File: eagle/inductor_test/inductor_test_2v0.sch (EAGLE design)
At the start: 22 parts, among them J1 MA02-1_ROUND

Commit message: added new amplifiers for inductor inspector
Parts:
- removed L10, L6, L7, L8, L9: (no value), rcl:L-USL0805
- added C1, C2, C3: (no value), rcl:C-EUC0603
- added R2, R3, R4, R5, R6, R7: (no value), rcl:R-US_R0603
- added U1: MCP6V3, powerfilm:MCP6V3
- added U2, U3: OPA333, powerfilm:MCP6V3
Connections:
- new net +3V3: C1.1, C2.1, C3.1, U1.VCC, U2.VCC, U3.VCC
- new net GND: C1.2, C2.2, C3.2, R4.1, R5.1, R7.1, U1.VSS, U2.VSS, U3.VSS
- new net L_SIG: U1.IN+, U2.IN+, U3.IN+
- new net N$3: R6.1, R7.2, U3.IN-
- new net N$4: R2.1, R4.2, U1.IN-
- new net N$6: R3.1, R5.2, U2.IN-
- new net OUT_MCP6V3: R2.2, U1.OUT
- new net OUT_OPA333: R3.2, R6.2, U2.OUT, U3.OUT
- net C1P1: no longer L14.1
- net C2P1: no longer L15.1
- net L10P1: no longer L10.1
- net L10P2: no longer L10.2
- net L11P1: now also L1.1, L12.1, L13.1, L14.1, L15.1, L2.1, L3.1, L4.1, L5.1
- net L12P1: no longer L12.1
- net L13P1: no longer L13.1
- net L1P1: no longer L1.1
- net L2P1: no longer L2.1
- net L3P1: no longer L3.1
- net L4P1: no longer L4.1
- net L5P1: no longer L5.1
- net L6P1: no longer L6.1
- net L6P2: no longer L6.2
- net L7P1: no longer L7.1
- net L7P2: no longer L7.2
- net L8P1: no longer L8.1
- net L8P2: no longer L8.2
- net L9P1: no longer L9.1
- net L9P2: no longer L9.2

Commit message: more work in inductor board
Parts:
- added C4, C5, C6, C7, C8: (no value), rcl:C-EUC0603
- added R10, R11, R8, R9: (no value), rcl:R-US_R0603
- added U4, U6: MAX4238, powerfilm:MAX4238
- added U5: LMP2014, powerfilm:LMP2014
- added U7: OPA376, powerfilm:MCP6V3
- U2: DIGIKEY (none) -> 296-19547-1-ND
- U3: value OPA333 -> OPA376; DIGIKEY (none) -> 296-22191-1-ND
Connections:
- new net N$5: R8.2, R9.1, U4.IN-
- new net N$7: C8.2, U7.IN+
- new net N$8: R10.1, R11.2, U5G1.IN-
- new net N$9: C6.2, U6.IN+
- new net OUT1_LMP2014: R10.2, U5G1.OUT
- new net OUT1_MAX4238: C6.1, R9.2, U4.OUT
- new net OUT1_OPA376: C8.1, R6.2, U3.OUT
- net +3V3: now also C4.1, C5.1, U4.VCC, U5G1.VCC
- net GND: now also C4.2, C5.2, R11.1, R8.1, U4.VSS, U5G1.VSS
- net L_SIG: now also U4.IN+
- net OUT_OPA333: no longer R6.2, U3.OUT

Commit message: added new amplifier configuration
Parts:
- removed J1, SV2, SV3: MA02-1_ROUND, con-lstb:MA02-1_ROUND
- removed L11, L12, L13, L14, L15: (no value), rcl:L-USL0805
- removed SV1: (no value), con-lstb:MA13-2BARE
- removed TP1, TP2: TP_STD, skyspecs:TP_STD
- removed U2: OPA333, powerfilm:MCP6V3
- removed U6: MAX4238, powerfilm:MAX4238
- removed U7: OPA376, powerfilm:MCP6V3
- added C10, C11, C12, C13, C9: (no value), rcl:C-EUC0402
- added C14: (no value), rcl:C-EUC0603
- added R12, R13, R14, R15, R16, R17, R18, R19: (no value), rcl:R-US_R0402
- C1, C2, C6, C7, C8: device rcl:C-EUC0603 -> rcl:C-EUC0402
- R1: device rcl:R-US_R0603 -> rcl:R-US_R0402; DIGIKEY P49.9HCT-ND -> (none); DIGIKEY_2 P220JCT-ND -> (none)
- R10, R11, R5, R6, R7, R8, R9: device rcl:R-US_R0603 -> rcl:R-US_R0402
- R2: value (none) -> 200; device rcl:R-US_R0603 -> rcl:R-US_R0402
- R3: value (none) -> 1M; device rcl:R-US_R0603 -> rcl:R-US_R0402
- R4: value (none) -> 75; device rcl:R-US_R0603 -> rcl:R-US_R0402
- U1: value MCP6V3 -> OPA2369; device powerfilm:MCP6V3 -> powerfilm:OPA2369
- U3: value OPA376 -> SC70
- U4: value MAX4238 -> SOT-23-6
- U5: value LMP2014 -> TSSOP-14
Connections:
- net OUT1_MAX4238 renamed OUT1_SOT23
- net OUT1_OPA376 renamed OUT1_SC70
- removed net C1P1: SV2.1
- removed net C1P2: L14.2, SV2.2
- removed net C2P1: SV3.2
- removed net C2P2: L15.2, SV3.1
- removed net L10P1: SV1.8
- removed net L10P2: SV1.7
- removed net L11P1: L1.1, L11.1, L12.1, L13.1, L14.1, L15.1, L2.1, L3.1, L4.1, L5.1, SV1.5
- removed net L11P2: L11.2, SV1.6
- removed net L12P1: SV1.4
- removed net L12P2: L12.2, SV1.3
- removed net L13P1: SV1.1
- removed net L13P2: L13.2, SV1.2
- removed net L1P1: SV1.25
- removed net L2P1: SV1.24
- removed net L2P2: L2.2, SV1.23
- removed net L3P1: SV1.21
- removed net L3P2: L3.2, SV1.22
- removed net L4P1: SV1.20
- removed net L4P2: L4.2, SV1.19
- removed net L5P1: SV1.17
- removed net L5P2: L5.2, SV1.18
- removed net L6P1: SV1.16
- removed net L6P2: SV1.15
- removed net L7P1: SV1.13
- removed net L7P2: SV1.14
- removed net L8P1: SV1.12
- removed net L8P2: SV1.11
- removed net L9P1: SV1.9
- removed net L9P2: SV1.10
- removed net OUT1_LMP2014: R10.2, U5G1.OUT
- removed net OUT_MCP6V3: R2.2, U1.OUT
- removed net OUT_OPA333: R3.2, U2.OUT
- new net N$10: C6.2, R12.1, U1G$2.IN+
- new net N$11: C11.1, R15.1
- new net N$12: C7.2, R13.1, U5G2.IN+
- new net N$14: R16.1, R17.2, U1G$2.IN-
- new net N$15: C12.1, R17.1
- new net N$17: R18.1, R19.2, U5G2.IN-
- new net N$18: C13.1, R19.1
- new net OUT1_TSSOP14: C7.1, R10.2, U5G1.OUT
- new net OUT2_SC70: R14.2, U1G$1.OUT
- new net OUT2_SOT23: R16.2, U1G$2.OUT
- new net OUT2_TSSOP14: R18.2, U5G2.OUT
- new net VREF_1V65: R5.2
- new net VREF_V054: R1.2, R12.2, R13.2
- net +3V3: now also C14.1, R3.1, U1G$1.VCC; no longer C1.1, C2.1, U1.VCC, U2.VCC
- net GND: now also C10.2, C11.2, C12.2, C13.2, C14.2, C9.2, U1G$1.VSS; no longer C1.2, R11.1, R5.1, R7.1, R8.1, U1.VSS, U2.VSS
- net L1P2: now also L2.2, L3.2, L4.2, L5.2, R2.1, R3.2, R4.2; no longer SV1.26
- net L_SIG: now also C1.2, R5.1, U5G1.IN+; no longer U1.IN+, U2.IN+
- net N$1: now also C10.1, R11.1; no longer J1.2, R1.1, TP1.P$1
- net N$2: now also C9.1, R8.1; no longer J1.1, R1.2, TP2.P$1
- net N$4: now also C1.1, L1.1, L2.1, L3.1, L4.1, L5.1, R2.2; no longer R2.1, R4.2, U1.IN-
- net N$6: now also C2.1, R7.1; no longer R3.1, R5.2, U2.IN-
- net N$7: now also R1.1, U1G$1.IN+; no longer U7.IN+
- net N$9: now also R14.1, R15.2, U1G$1.IN-; no longer C6.2, U6.IN+
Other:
- note added: "New Configuration:"
- note added: "Old Configuration:"

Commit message: added all components for inductor inspector
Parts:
- added C15: (no value), rcl:C-EUC0402
- added R20, R21, R22, R23: (no value), rcl:R-US_R0402
- added TP1, TP10, TP11, TP12, TP13, TP14, TP2, TP3, TP4, TP5, TP6, TP7, TP8, TP9: TP_MULT, skyspecs:TP_MULT
- added U2: OPA2369, powerfilm:OPA2369
- C3: device rcl:C-EUC0603 -> rcl:C-EUC0402
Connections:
- new net N$13: R22.1, R23.2, U2G$2.IN+
- new net N$16: R20.2, R21.1, U2G$1.IN+
- net +3V3: now also C15.1, R21.2, R22.2, U2G$1.VCC
- net GND: now also C15.2, R20.1, R23.1, TP10.P$1, TP11.P$1, TP12.P$1, TP13.P$1, TP14.P$1, TP9.P$1, U2G$1.VSS
- net OUT1_SC70: now also TP1.P$1
- net OUT1_SOT23: now also TP3.P$1
- net OUT1_TSSOP14: now also TP5.P$1
- net OUT2_SC70: now also TP2.P$1
- net OUT2_SOT23: now also TP4.P$1
- net OUT2_TSSOP14: now also TP6.P$1
- net VREF_1V65: now also TP7.P$1, U2G$1.IN-, U2G$1.OUT
- net VREF_V054: now also TP8.P$1, U2G$2.IN-, U2G$2.OUT

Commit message: all components added for inductor inspector
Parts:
- removed TP14: TP_MULT, skyspecs:TP_MULT
- added C16: 22pF, rcl:C-EUC0402_SM
- added C17: 4.7uF, rcl:C-EUC0402_SM
- added C18, C19: 0.1uF, rcl:C-EUC0402_SM
- added C20, C21: 22uF, rcl:C-EUC0603_SM
- added C22: 0.1uF, rcl:C-EUC0603
- added J1: MA02-1, con-lstb:MA02-1
- added L6: 10uH, rcl:L-USL0805
- added R24: 560k, rcl:R-US_R0402_SM
- added R25: 180k, rcl:R-US_R0402_SM
- added R26: 1 1%, rcl:R-US_R0603_SM
- added R27, R28: 10k, rcl:R-US_R0603
- added R29, R30: 10, rcl:R-US_R0603
- added TP16: TP_MULT, skyspecs:TP_MULT
- added U6: TPS62122, powerfilm:TPS62122
- added U7: MAX9910, powerfilm:MAX9910
- C14, C4, C5: device rcl:C-EUC0603 -> rcl:C-EUC0402
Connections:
- new net N$19: C16.2, R24.1, R25.2, U6.FB
- new net N$20: L6.2, U6.SW
- new net N$21: R28.1, R29.2, U7.IN+
- new net N$22: R27.1, R30.2, U7.IN-
- new net N$23: R27.2, TP16.P$1, U7.OUT
- new net VCC: C17.1, C18.1, J1.1, U6.EN, U6.VIN
- new net VS+: C16.1, C19.1, C20.1, L6.1, R24.2, R26.1, R29.1, U6.VOUT
- net +3V3: now also C21.1, C22.1, R26.2, R30.1, U7.VCC
- net GND: now also C17.2, C18.2, C19.2, C20.2, C21.2, C22.2, J1.2, R25.1, R28.2, U6.GND, U7.VSS; no longer TP14.P$1

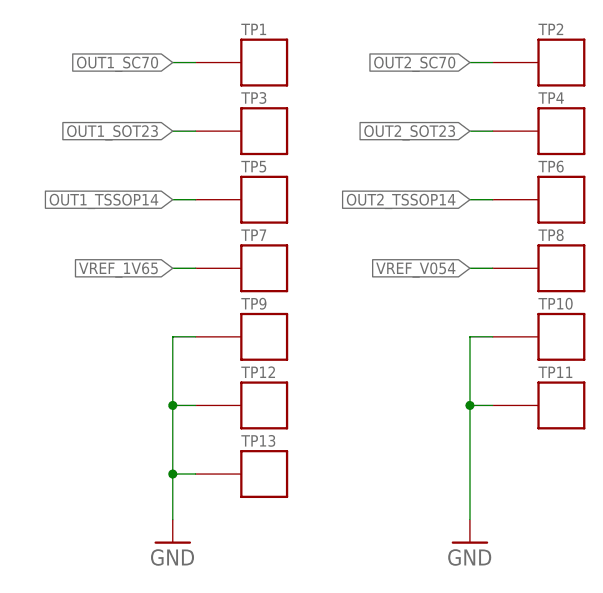
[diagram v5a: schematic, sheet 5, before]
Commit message: 23 airwires left
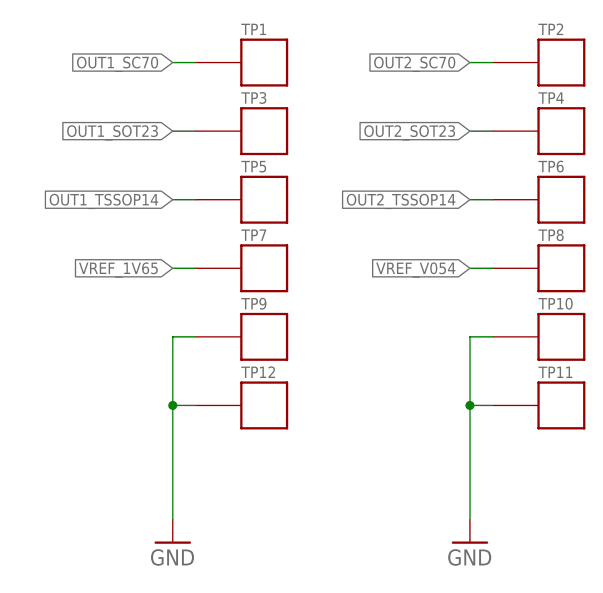
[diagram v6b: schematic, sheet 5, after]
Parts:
- removed TP13: TP_MULT, skyspecs:TP_MULT
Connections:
- net GND: no longer TP13.P$1
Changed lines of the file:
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@@
 <?xml version="1.0" encoding="utf-8"?>
 <!DOCTYPE eagle SYSTEM "eagle.dtd">
-<eagle version="6.3">
+<eagle version="6.5.0">
 <drawing>
 <settings>
@@
 <grid distance="0.1" unitdist="inch" unit="inch" style="lines" multiple="1" display="no" altdistance="0.01" altunitdist="inch" altunit="inch"/>
 <layers>
-<layer number="1" name="Top" color="4" fill="1" visible="yes" active="no"/>
-<layer number="2" name="Route2" color="1" fill="3" visible="yes" active="no"/>
-<layer number="3" name="Route3" color="4" fill="3" visible="yes" active="no"/>
-<layer number="4" name="Route4" color="1" fill="4" visible="yes" active="no"/>
-<layer number="5" name="Route5" color="4" fill="4" visible="yes" active="no"/>
-<layer number="6" name="Route6" color="1" fill="8" visible="yes" active="no"/>
-<layer number="7" name="Route7" color="4" fill="8" visible="yes" active="no"/>
-<layer number="8" name="Route8" color="1" fill="2" visible="yes" active="no"/>
-<layer number="9" name="Route9" color="4" fill="2" visible="yes" active="no"/>
-<layer number="10" name="Route10" color="1" fill="7" visible="yes" active="no"/>
-<layer number="11" name="Route11" color="4" fill="7" visible="yes" active="no"/>
-<layer number="12" name="Route12" color="1" fill="5" visible="yes" active="no"/>
-<layer number="13" name="Route13" color="4" fill="5" visible="yes" active="no"/>
-<layer number="14" name="Route14" color="1" fill="6" visible="yes" active="no"/>
-<layer number="15" name="Route15" color="4" fill="6" visible="yes" active="no"/>
-<layer number="16" name="Bottom" color="1" fill="1" visible="yes" active="no"/>
-<layer number="17" name="Pads" color="2" fill="1" visible="yes" active="no"/>
-<layer number="18" name="Vias" color="2" fill="1" visible="yes" active="no"/>
-<layer number="19" name="Unrouted" color="6" fill="1" visible="yes" active="no"/>
-<layer number="20" name="Dimension" color="15" fill="1" visible="yes" active="no"/>
-<layer number="21" name="tPlace" color="7" fill="1" visible="yes" active="no"/>
-<layer number="22" name="bPlace" color="7" fill="1" visible="yes" active="no"/>
-<layer number="23" name="tOrigins" color="15" fill="1" visible="yes" active="no"/>
-<layer number="24" name="bOrigins" color="15" fill="1" visible="yes" active="no"/>
-<layer number="25" name="tNames" color="7" fill="1" visible="yes" active="no"/>
-<layer number="26" name="bNames" color="7" fill="1" visible="yes" active="no"/>
-<layer number="27" name="tValues" color="7" fill="1" visible="yes" active="no"/>
-<layer number="28" name="bValues" color="7" fill="1" visible="yes" active="no"/>
+<layer number="1" name="Top" color="4" fill="1" visible="no" active="no"/>
+<layer number="2" name="Route2" color="1" fill="3" visible="no" active="no"/>
+<layer number="3" name="Route3" color="4" fill="3" visible="no" active="no"/>
+<layer number="4" name="Route4" color="1" fill="4" visible="no" active="no"/>
+<layer number="5" name="Route5" color="4" fill="4" visible="no" active="no"/>
+<layer number="6" name="Route6" color="1" fill="8" visible="no" active="no"/>
+<layer number="7" name="Route7" color="4" fill="8" visible="no" active="no"/>
+<layer number="8" name="Route8" color="1" fill="2" visible="no" active="no"/>
+<layer number="9" name="Route9" color="4" fill="2" visible="no" active="no"/>
+<layer number="10" name="Route10" color="1" fill="7" visible="no" active="no"/>
+<layer number="11" name="Route11" color="4" fill="7" visible="no" active="no"/>
+<layer number="12" name="Route12" color="1" fill="5" visible="no" active="no"/>
+<layer number="13" name="Route13" color="4" fill="5" visible="no" active="no"/>
+<layer number="14" name="Route14" color="1" fill="6" visible="no" active="no"/>
+<layer number="15" name="Route15" color="4" fill="6" visible="no" active="no"/>
+<layer number="16" name="Bottom" color="1" fill="1" visible="no" active="no"/>
+<layer number="17" name="Pads" color="2" fill="1" visible="no" active="no"/>
+<layer number="18" name="Vias" color="2" fill="1" visible="no" active="no"/>
+<layer number="19" name="Unrouted" color="6" fill="1" visible="no" active="no"/>
+<layer number="20" name="Dimension" color="15" fill="1" visible="no" active="no"/>
+<layer number="21" name="tPlace" color="7" fill="1" visible="no" active="no"/>
+<layer number="22" name="bPlace" color="7" fill="1" visible="no" active="no"/>
+<layer number="23" name="tOrigins" color="15" fill="1" visible="no" active="no"/>
+<layer number="24" name="bOrigins" color="15" fill="1" visible="no" active="no"/>
+<layer number="25" name="tNames" color="7" fill="1" visible="no" active="no"/>
+<layer number="26" name="bNames" color="7" fill="1" visible="no" active="no"/>
+<layer number="27" name="tValues" color="7" fill="1" visible="no" active="no"/>
+<layer number="28" name="bValues" color="7" fill="1" visible="no" active="no"/>
 <layer number="29" name="tStop" color="7" fill="3" visible="no" active="no"/>
 <layer number="30" name="bStop" color="7" fill="6" visible="no" active="no"/>
@@
 <layer number="35" name="tGlue" color="7" fill="4" visible="no" active="no"/>
 <layer number="36" name="bGlue" color="7" fill="5" visible="no" active="no"/>
-<layer number="37" name="tTest" color="7" fill="1" visible="yes" active="no"/>
-<layer number="38" name="bTest" color="7" fill="1" visible="yes" active="no"/>
+<layer number="37" name="tTest" color="7" fill="1" visible="no" active="no"/>
+<layer number="38" name="bTest" color="7" fill="1" visible="no" active="no"/>
 <layer number="39" name="tKeepout" color="4" fill="11" visible="no" active="no"/>
 <layer number="40" name="bKeepout" color="1" fill="11" visible="no" active="no"/>
@@
 <layer number="44" name="Drills" color="7" fill="1" visible="no" active="no"/>
 <layer number="45" name="Holes" color="7" fill="1" visible="no" active="no"/>
-<layer number="46" name="Milling" color="3" fill="1" visible="yes" active="no"/>
-<layer number="47" name="Measures" color="7" fill="1" visible="yes" active="no"/>
-<layer number="48" name="Document" color="7" fill="1" visible="yes" active="no"/>
-<layer number="49" name="Reference" color="7" fill="1" visible="yes" active="no"/>
-<layer number="50" name="dxf" color="7" fill="1" visible="yes" active="no"/>
-<layer number="51" name="tDocu" color="7" fill="1" visible="yes" active="no"/>
-<layer number="52" name="bDocu" color="7" fill="1" visible="yes" active="no"/>
-<layer number="53" name="tGND_GNDA" color="7" fill="9" visible="yes" active="no"/>
-<layer number="54" name="bGND_GNDA" color="1" fill="9" visible="yes" active="no"/>
-<layer number="56" name="wert" color="7" fill="1" visible="yes" active="no"/>
-<layer number="57" name="tCAD" color="7" fill="1" visible="yes" active="no"/>
+<layer number="46" name="Milling" color="3" fill="1" visible="no" active="no"/>
+<layer number="47" name="Measures" color="7" fill="1" visible="no" active="no"/>
+<layer number="48" name="Document" color="7" fill="1" visible="no" active="no"/>
+<layer number="49" name="Reference" color="7" fill="1" visible="no" active="no"/>
+<layer number="50" name="dxf" color="7" fill="1" visible="no" active="no"/>
+<layer number="51" name="tDocu" color="7" fill="1" visible="no" active="no"/>
+<layer number="52" name="bDocu" color="7" fill="1" visible="no" active="no"/>
+<layer number="53" name="tGND_GNDA" color="7" fill="9" visible="no" active="no"/>
+<layer number="54" name="bGND_GNDA" color="1" fill="9" visible="no" active="no"/>
+<layer number="56" name="wert" color="7" fill="1" visible="no" active="no"/>
+<layer number="57" name="tCAD" color="7" fill="1" visible="no" active="no"/>
 <layer number="91" name="Nets" color="2" fill="1" visible="yes" active="yes"/>
 <layer number="92" name="Busses" color="1" fill="1" visible="yes" active="yes"/>
@@
 <part name="TP11" library="skyspecs" deviceset="TP" device="_MULT"/>
 <part name="TP12" library="skyspecs" deviceset="TP" device="_MULT"/>
-<part name="TP13" library="skyspecs" deviceset="TP" device="_MULT"/>
 <part name="GND20" library="supply1" deviceset="GND" device=""/>
 <part name="GND21" library="supply1" deviceset="GND" device=""/>
@@
 <instance part="TP11" gate="G$1" x="17.78" y="-27.94"/>
 <instance part="TP12" gate="G$1" x="-15.24" y="-27.94"/>
-<instance part="TP13" gate="G$1" x="-15.24" y="-35.56"/>
 <instance part="GND20" gate="1" x="10.16" y="-43.18"/>
 <instance part="GND21" gate="1" x="-22.86" y="-43.18"/>
@@
 <wire x1="-20.32" y1="-20.32" x2="-22.86" y2="-20.32" width="0.1524" layer="91"/>
 <wire x1="-22.86" y1="-20.32" x2="-22.86" y2="-27.94" width="0.1524" layer="91"/>
-<pinref part="TP13" gate="G$1" pin="P$1"/>
-<wire x1="-22.86" y1="-27.94" x2="-22.86" y2="-35.56" width="0.1524" layer="91"/>
-<wire x1="-22.86" y1="-35.56" x2="-22.86" y2="-40.64" width="0.1524" layer="91"/>
-<wire x1="-20.32" y1="-35.56" x2="-22.86" y2="-35.56" width="0.1524" layer="91"/>
-<junction x="-22.86" y="-35.56"/>
+<wire x1="-22.86" y1="-27.94" x2="-22.86" y2="-40.64" width="0.1524" layer="91"/>
 <pinref part="TP12" gate="G$1" pin="P$1"/>
 <wire x1="-20.32" y1="-27.94" x2="-22.86" y2="-27.94" width="0.1524" layer="91"/>

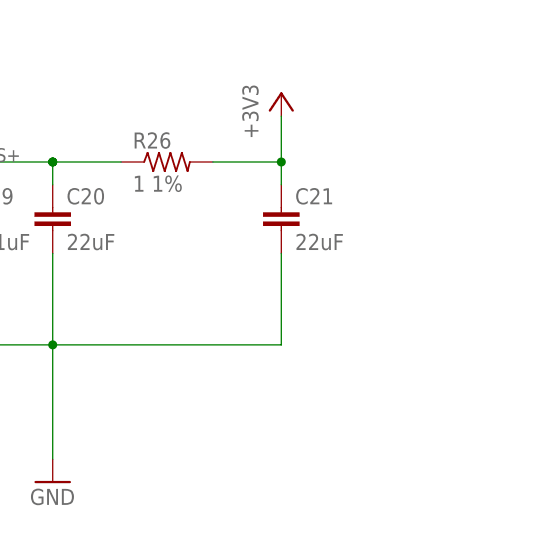
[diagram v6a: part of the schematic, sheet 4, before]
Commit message: added pogo pin to inductor test board
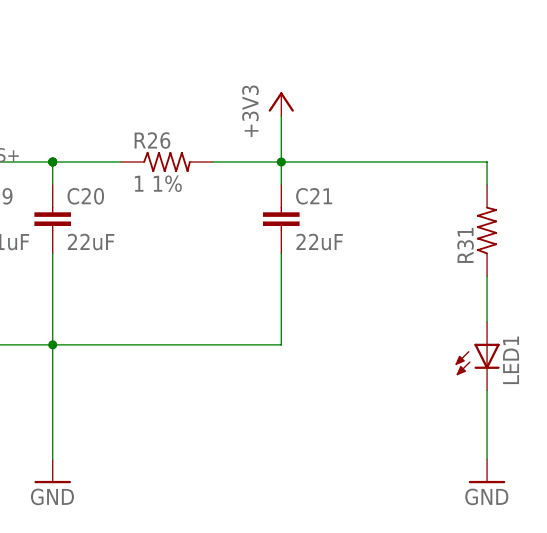
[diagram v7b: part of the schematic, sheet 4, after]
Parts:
- added LED1: (no value), SparkFun-LED:LED3MM
- added R31: (no value), rcl:R-US_R0603
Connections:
- new net N$24: LED1.A, R31.1
- net +3V3: now also R31.2
- net GND: now also LED1.C
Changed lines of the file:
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@@
 <part name="GND28" library="supply1" deviceset="GND" device=""/>
 <part name="+3V11" library="supply1" deviceset="+3V3" device=""/>
+<part name="R31" library="rcl" deviceset="R-US_" device="R0603"/>
+<part name="LED1" library="SparkFun-LED" deviceset="LED" device="3MM"/>
+<part name="GND29" library="supply1" deviceset="GND" device=""/>
 </parts>
 <sheets>
@@
 <instance part="GND28" gate="1" x="76.2" y="73.66"/>
 <instance part="+3V11" gate="G$1" x="30.48" y="73.66"/>
+<instance part="R31" gate="G$1" x="111.76" y="-2.54" rot="R90"/>
+<instance part="LED1" gate="G$1" x="111.76" y="-15.24"/>
+<instance part="GND29" gate="1" x="111.76" y="-30.48"/>
 </instances>
 <busses>
@@
 <pinref part="GND27" gate="1" pin="GND"/>
 <wire x1="83.82" y1="55.88" x2="83.82" y2="53.34" width="0.1524" layer="91"/>
+</segment>
+<segment>
+<pinref part="LED1" gate="G$1" pin="C"/>
+<pinref part="GND29" gate="1" pin="GND"/>
+<wire x1="111.76" y1="-20.32" x2="111.76" y2="-27.94" width="0.1524" layer="91"/>
 </segment>
 </net>
@@
 <pinref part="C21" gate="G$1" pin="1"/>
 <wire x1="88.9" y1="2.54" x2="88.9" y2="5.08" width="0.1524" layer="91"/>
+<pinref part="R31" gate="G$1" pin="2"/>
+<wire x1="88.9" y1="5.08" x2="111.76" y2="5.08" width="0.1524" layer="91"/>
+<wire x1="111.76" y1="5.08" x2="111.76" y2="2.54" width="0.1524" layer="91"/>
 </segment>
 <segment>
@@
 </segment>
 </net>
+<net name="N$24" class="0">
+<segment>
+<pinref part="R31" gate="G$1" pin="1"/>
+<pinref part="LED1" gate="G$1" pin="A"/>
+<wire x1="111.76" y1="-7.62" x2="111.76" y2="-12.7" width="0.1524" layer="91"/>
+</segment>
+</net>
